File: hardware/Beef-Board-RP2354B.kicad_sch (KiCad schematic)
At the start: 78 parts, among them J1 USB-C DEVICE, J10 VAUX OUT, J11 B1 LEGACY, J12 B2 LEGACY, J13 B3 LEGACY, J14 B4 LEGACY, J15 B5 LEGACY, J16 B6 LEGACY, J17 B7 LEGACY, J18 B8 LEGACY, J19 B9 LEGACY, J20 B10 LEGACY, J21 B11 LEGACY, J22 USB COMMON, J3 VAUX 5V INPUT, J31 ENCODER 1, J32 ENCODER 2, J33 AE1 0-5V, J34 AE2 0-5V, J4 USB-C AUX POWER, J40 TT RGB, J41 CENTER BAR RGB, J42 UART A 3V3, J43 UART B 3V3, J5 ENC1 A, J6 ENC1 B, J60 BOOTSEL HEADER, J61 RESET HEADER (RUN TO GND), J7 ENC2 A, J8 ENC2 B, J9 VAUX OUT, Q1 2N7002, Q10 2N7002, Q11 2N7002, Q2 2N7002, Q3 2N7002, Q4 2N7002, Q5 2N7002, Q6 2N7002, Q7 2N7002, Q8 2N7002, Q9 2N7002, SW2 BOOTSEL, U1 RP2354B, U2 USBLC6-2SC6, U3 AP2112K-3.3, Y1 12MHz CL=10pF

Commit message: Add power source selector to board and BOM
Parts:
- added SW1: POWER SELECT, Button_Switch_THT:SW_DIP_SPSTx01_Slide_9.78x4.72mm_W7.62mm_P2.54mm, symbol Switch:SW_SPST
- J1: footprint Connector_USB:USB_C_Receptacle_GCT_USB4105-xx-A_16P_TopMnt_Horizontal -> BEEF-BOARD:USB-C-TH_G-SWITCH_GT-USB-7038X_1
- J4: footprint Connector_USB:USB_C_Receptacle_G-Switch_GT-USB-7051x -> BEEF-BOARD:USB-C-TH_G-SWITCH_GT-USB-7038X_1
- J61: value RESET HEADER (RUN TO GND) -> RESET HEADER
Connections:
- net VAUX_5V: now also SW1.1 (A)
- net VBUS_5V: now also SW1.2 (B)
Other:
- note added: "DESIGN NOTES: RP2354B QFN-80; external 12 MHz crystal; USB 2.0 device."
- note added: "Reset is available on J61 (RUN to GND). BOOTSEL is available on J60; SW2 is not populated."
- note added: "SW1 connects J1 VBUS to VAUX when enabled. With SW1 off, J4 EXT_5V reaches VAUX through D1; JP1 is DNP."
- note added: "TT and Center RGB data connect directly to RP2354B GPIO at 3.3 V; no AHCT buffer is fitted."
- note added: "UART A and B connect directly to RP2354B GPIO; use 3.3 V logic."
- note added: "USB D+ and D- are routed through U2 USBLC6-2SC6 for ESD protection."
- note removed: "Both UART TX and RX are connected directly to STM32 GPIO and must use 3.3 V logic."
- note removed: "Connector placement is provisional because original Beef-Board dimensions/coordinates were not supplied."
- note removed: "DESIGN NOTES: STM32F303RCT6 LQFP64; HSE 8 MHz; USB FS device."
- note removed: "JP1 is open by default. Fit only when intentionally tying USB VBUS to VAUX; D1 prevents VAUX backfeed into EXT_5V."
- note removed: "No reset push button or SWD pin header is fitted; NRST keeps its 100nF capacitor."
- note removed: "TT and Center RGB data are driven directly from STM32 GPIO at 3.3 V; no AHCT buffer is fitted."
- note removed: "USB D+ requires external 1.5 kOhm pull-up to 3.0-3.6 V on this MCU family."

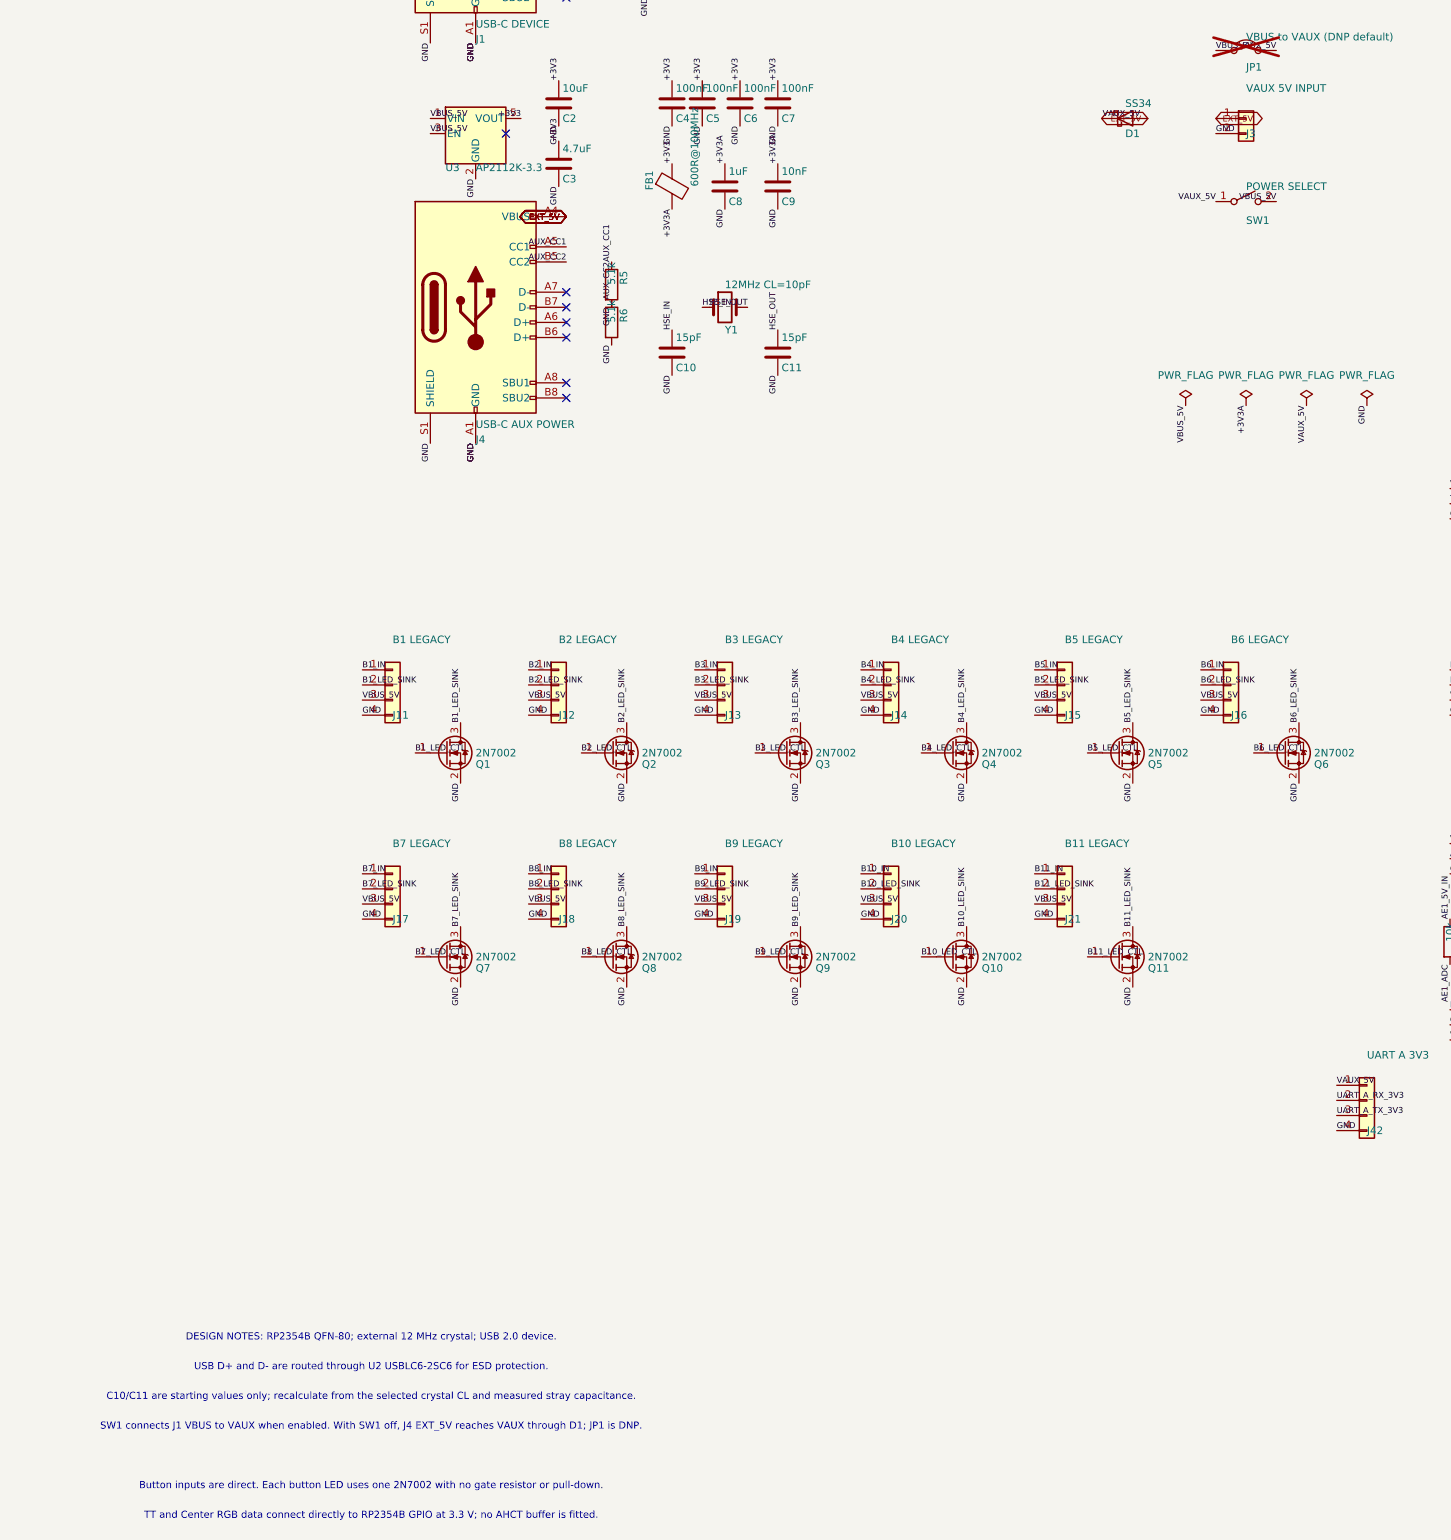
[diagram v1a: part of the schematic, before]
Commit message: Replace power switch with selectable header
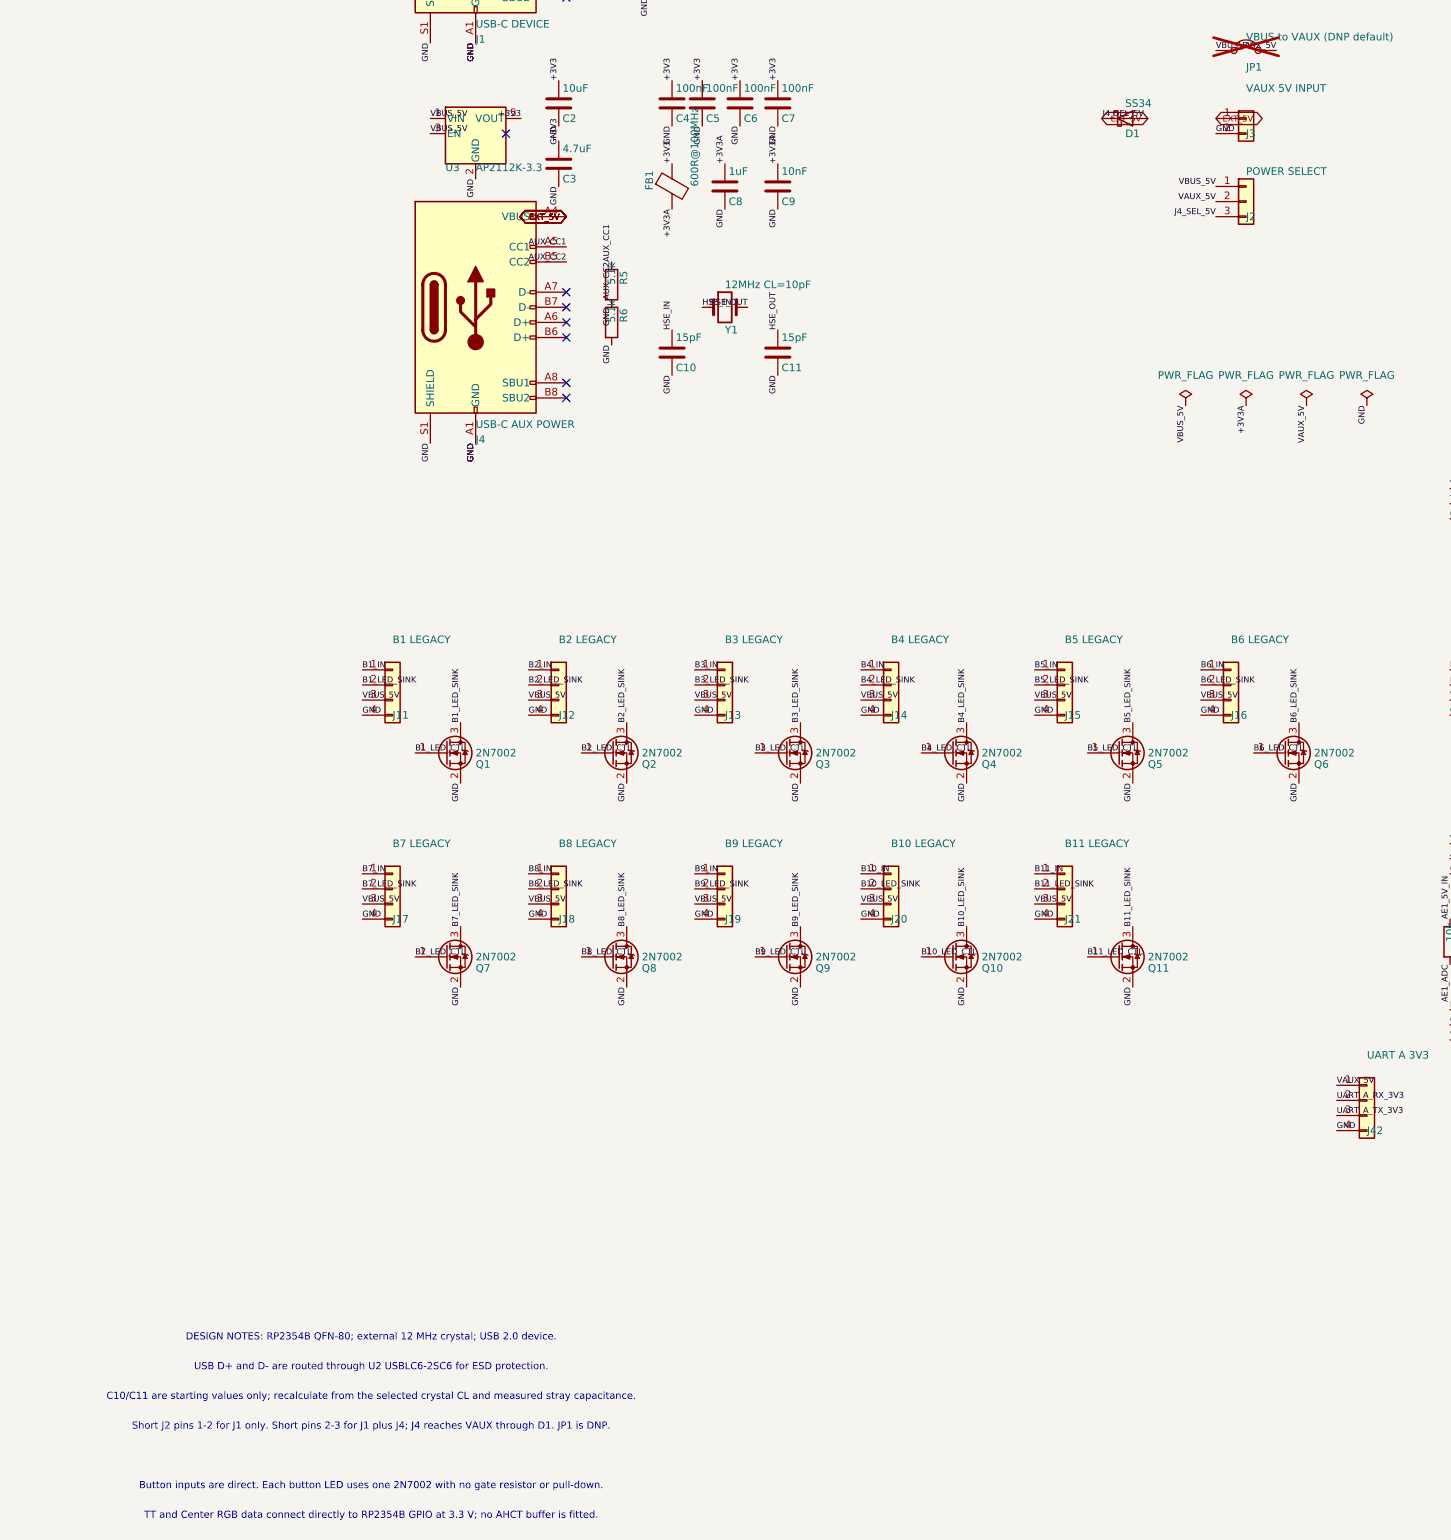
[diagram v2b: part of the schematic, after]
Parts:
- removed SW1: POWER SELECT, Button_Switch_THT:SW_DIP_SPSTx01_Slide_9.78x4.72mm_W7.62mm_P2.54mm, symbol Switch:SW_SPST
- added J2: POWER SELECT, Connector_PinHeader_2.54mm:PinHeader_1x03_P2.54mm_Vertical, symbol Connector_Generic:Conn_01x03
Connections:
- net VAUX_5V: now also J2.2 (Pin_2); no longer D1.1 (K)
- net VBUS_5V: now also J2.1 (Pin_1)
- new net J4_SEL_5V: D1.1 (K), J2.3 (Pin_3)
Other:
- note added: "Short J2 pins 1-2 for J1 only. Short pins 2-3 for J1 plus J4; J4 reaches VAUX through D1. JP1 is DNP."
- note removed: "SW1 connects J1 VBUS to VAUX when enabled. With SW1 off, J4 EXT_5V reaches VAUX through D1; JP1 is DNP."

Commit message: Revert "Replace power switch with selectable header"
This reverts commit b092bcadf7da63c17735a3d5c7bcba7038b5f74d.
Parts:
- removed J2: POWER SELECT, Connector_PinHeader_2.54mm:PinHeader_1x03_P2.54mm_Vertical, symbol Connector_Generic:Conn_01x03
- added SW1: POWER SELECT, Button_Switch_THT:SW_DIP_SPSTx01_Slide_9.78x4.72mm_W7.62mm_P2.54mm, symbol Switch:SW_SPST
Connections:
- net J4_SEL_5V is gone; now on net VAUX_5V: D1.1 (K)
- net VAUX_5V: now also SW1.1 (A)
- net VBUS_5V: now also SW1.2 (B)
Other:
- note added: "SW1 connects J1 VBUS to VAUX when enabled. With SW1 off, J4 EXT_5V reaches VAUX through D1; JP1 is DNP."
- note removed: "Short J2 pins 1-2 for J1 only. Short pins 2-3 for J1 plus J4; J4 reaches VAUX through D1. JP1 is DNP."

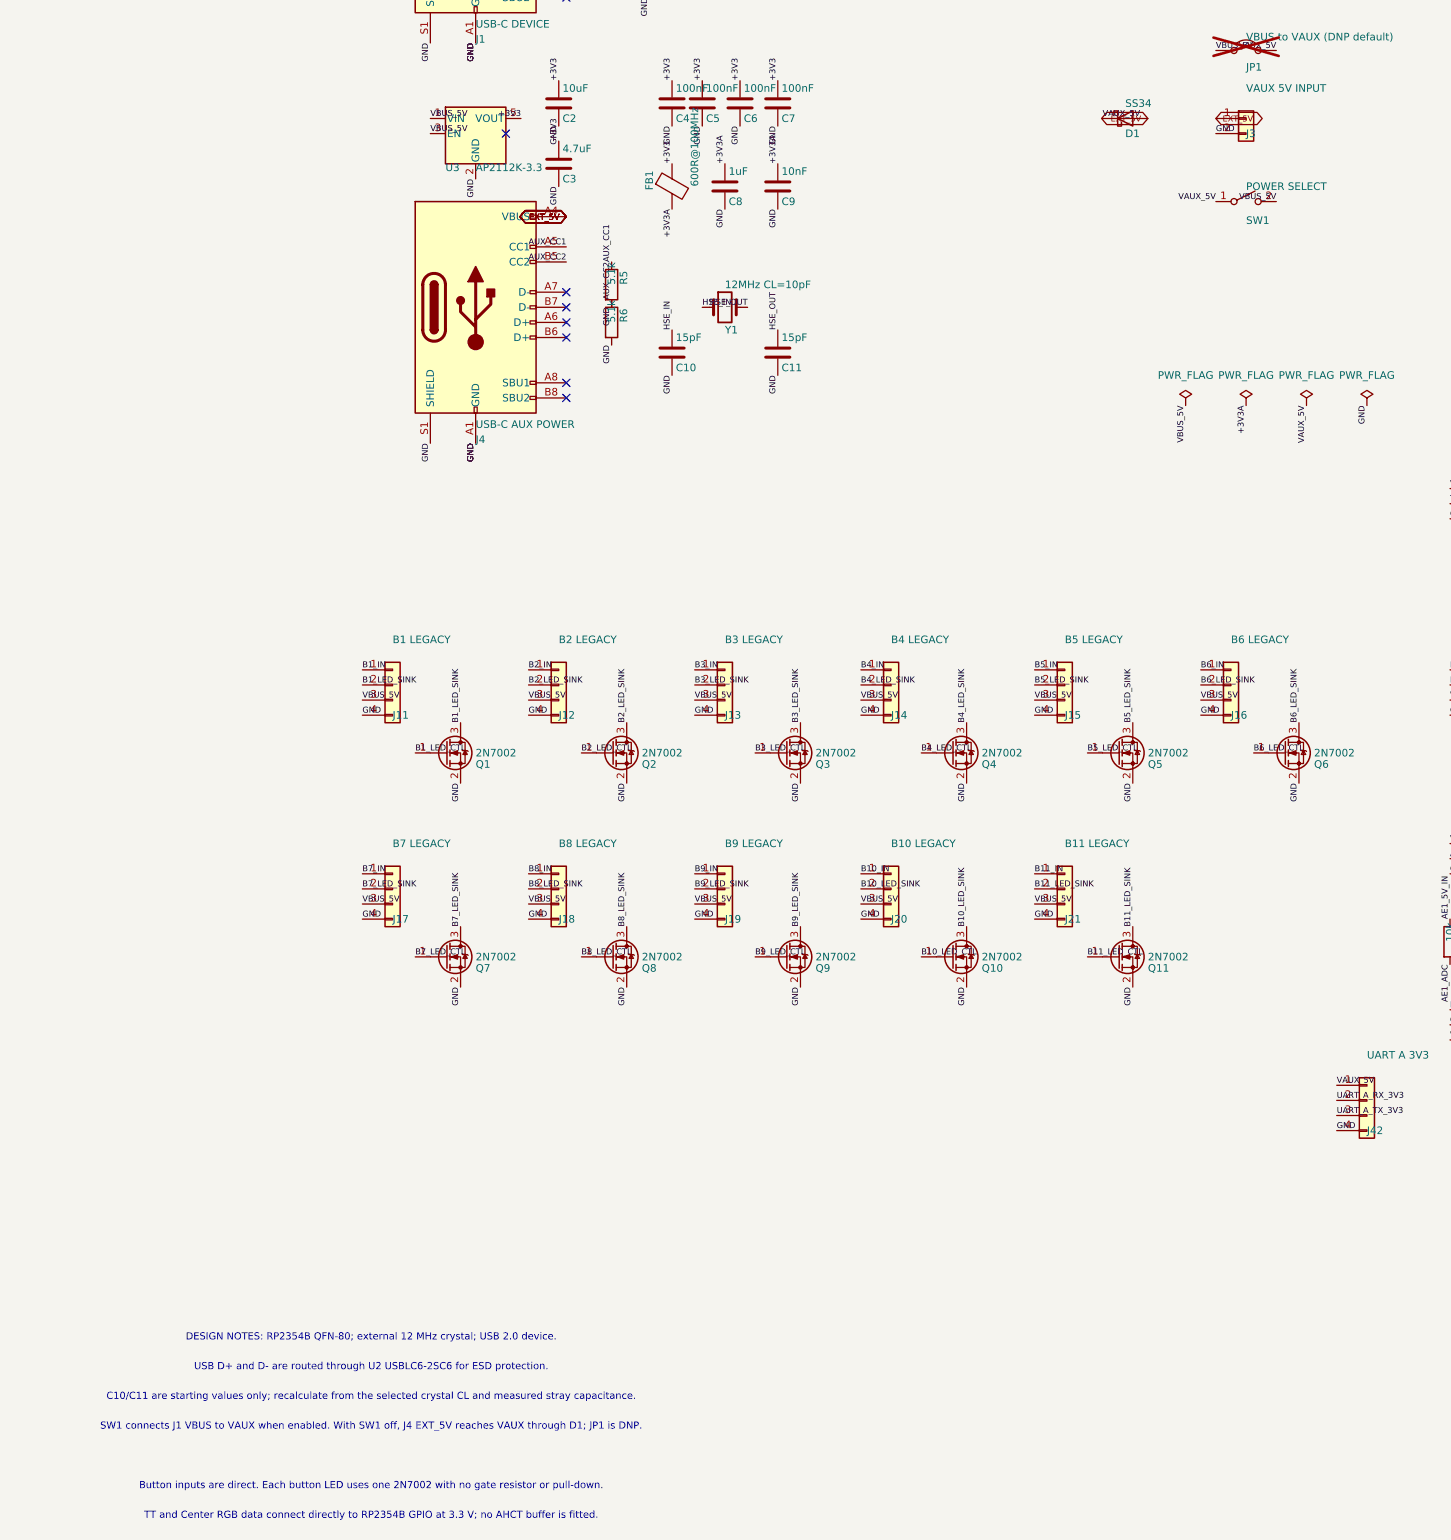
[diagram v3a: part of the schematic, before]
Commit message: Replace power selector with matched three-pin header
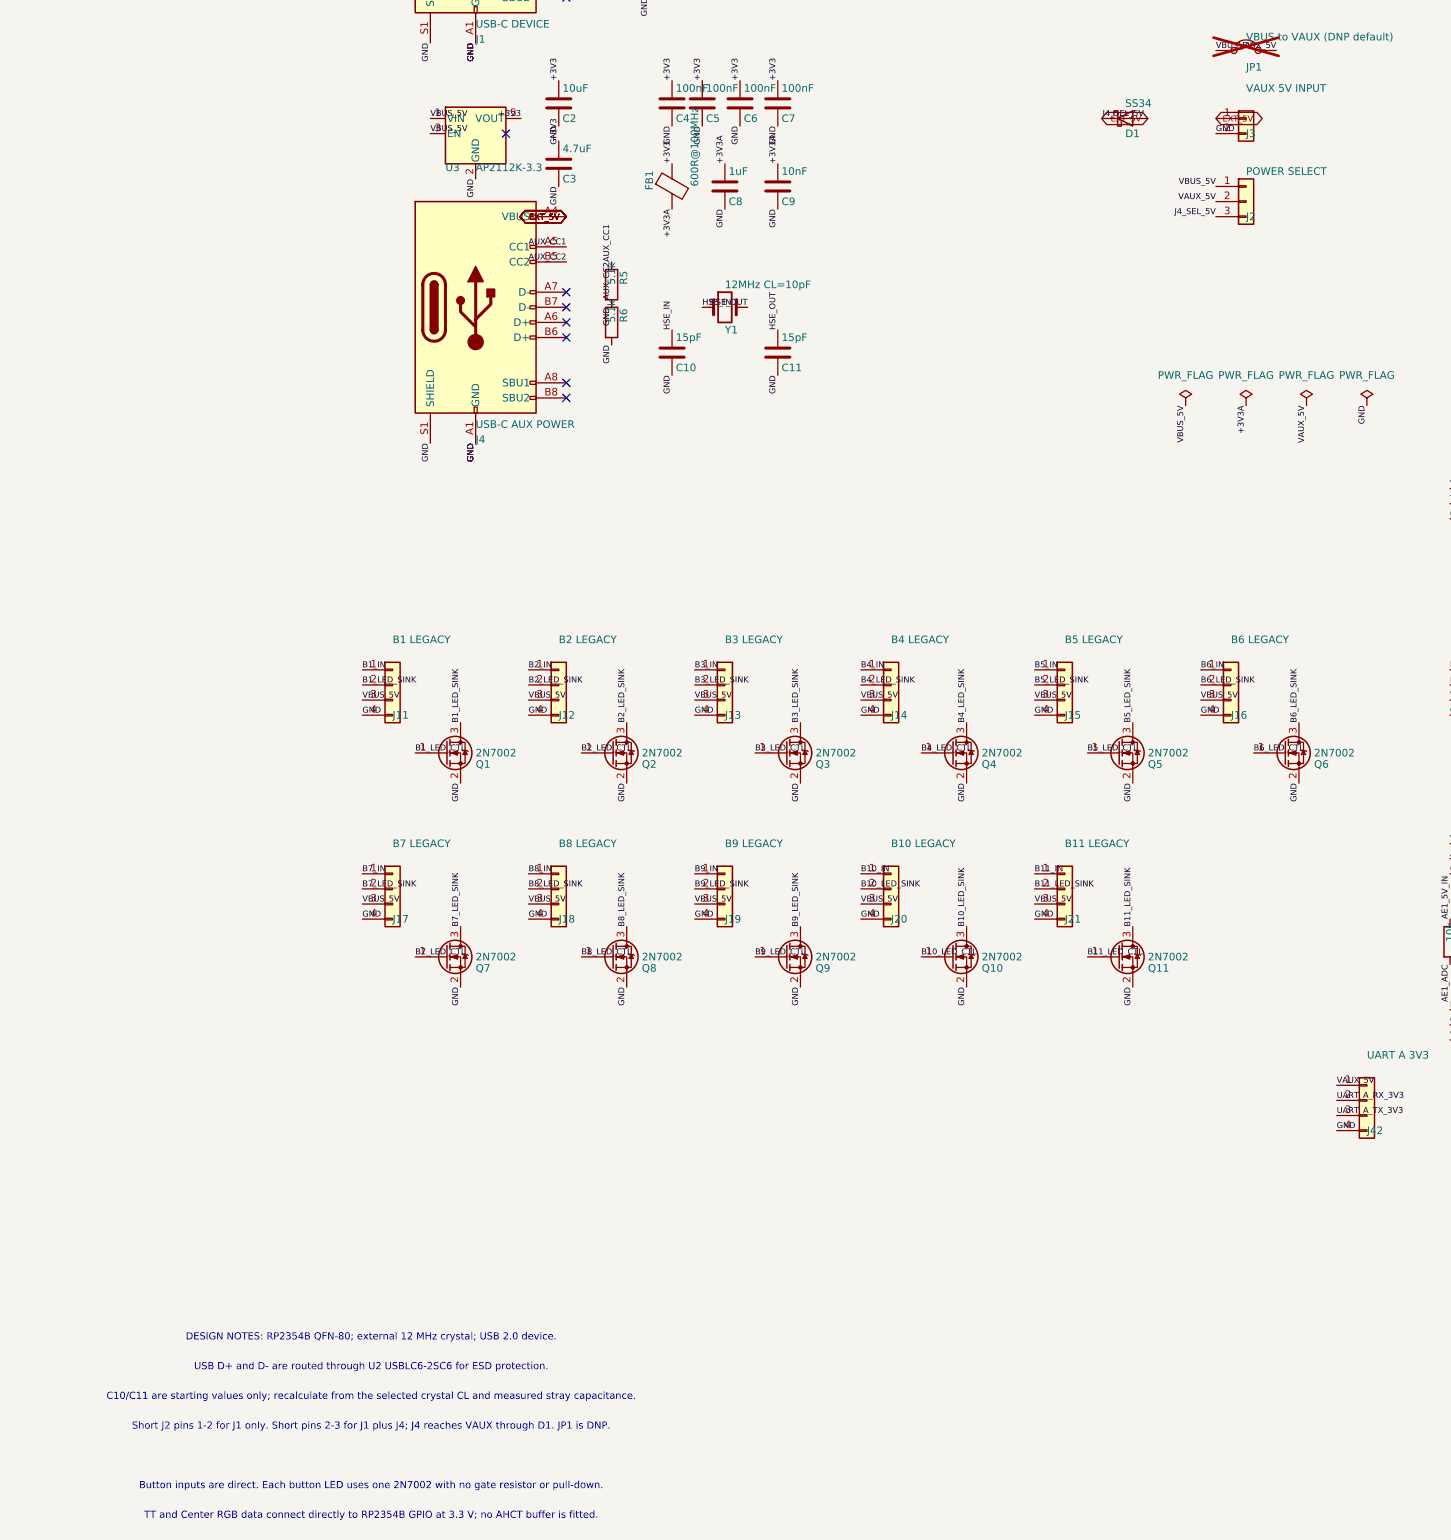
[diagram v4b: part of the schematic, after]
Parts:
- removed SW1: POWER SELECT, Button_Switch_THT:SW_DIP_SPSTx01_Slide_9.78x4.72mm_W7.62mm_P2.54mm, symbol Switch:SW_SPST
- added J2: POWER SELECT, Connector_PinHeader_2.54mm:PinHeader_1x03_P2.54mm_Vertical, symbol Connector_Generic:Conn_01x03
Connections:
- net VAUX_5V: now also J2.2 (Pin_2); no longer D1.1 (K)
- net VBUS_5V: now also J2.1 (Pin_1)
- new net J4_SEL_5V: D1.1 (K), J2.3 (Pin_3)
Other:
- note added: "Short J2 pins 1-2 for J1 only. Short pins 2-3 for J1 plus J4; J4 reaches VAUX through D1. JP1 is DNP."
- note removed: "SW1 connects J1 VBUS to VAUX when enabled. With SW1 off, J4 EXT_5V reaches VAUX through D1; JP1 is DNP."
